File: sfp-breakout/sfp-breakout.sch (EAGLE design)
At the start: 40 parts, among them J1 694108106102, T1 BC847, T2 BC847, U1 LDO-MCP1825S, X1 PINHD-1X5LOCK, X2 PINHD-1X5LOCK, X3 PINHD-1X4LOCK

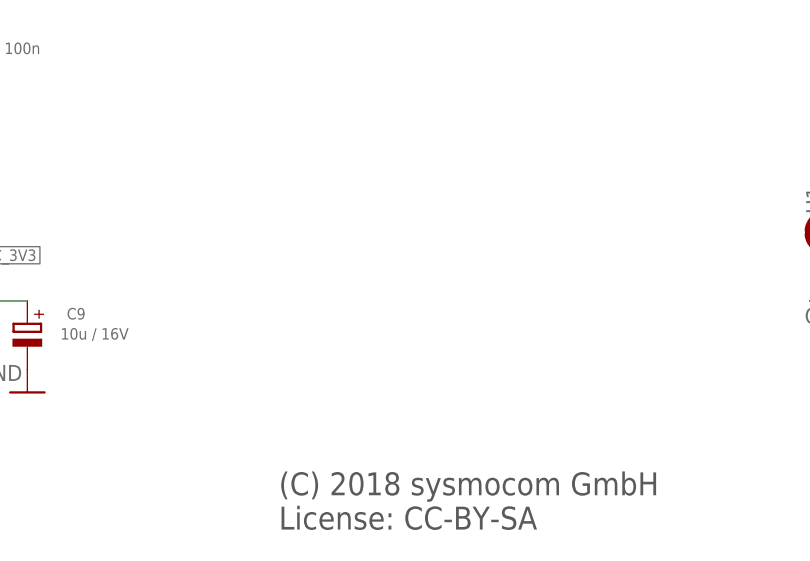
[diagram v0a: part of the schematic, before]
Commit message: sfp: add part numbers for SFP conn and cage
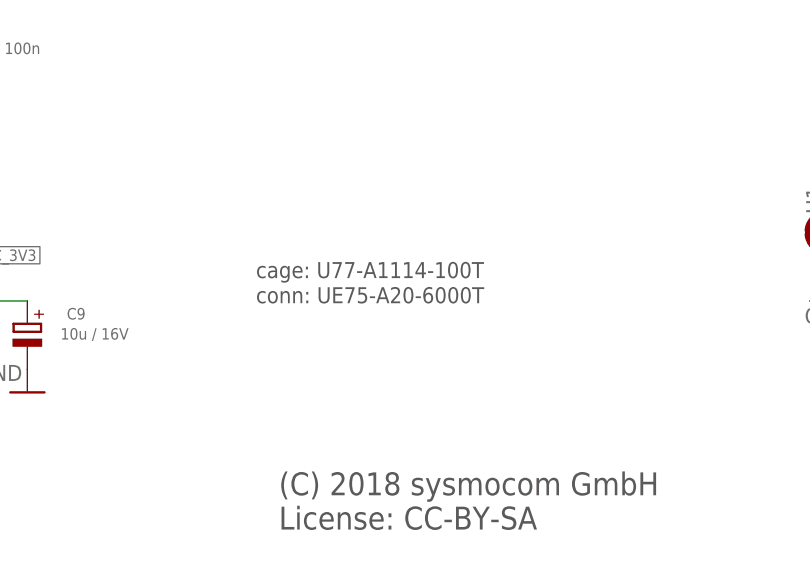
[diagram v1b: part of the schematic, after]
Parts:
- L1, L2: LINK UNKNOWN LINK -> https://www.digikey.de/product-detail/en/samsung-electro-me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
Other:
- note added: "cage: U77-A1114-100T"
- note added: "conn: UE75-A20-6000T"
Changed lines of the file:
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@@
 <attribute name="CLASS" value="INDUCTOR"/>
 <attribute name="DESCRIPTION" value="NO DESCRIPTION"/>
-<attribute name="LINK" value="UNKNOWN LINK"/>
+<attribute name="LINK" value="https://www.digikey.de/product-detail/en/samsung-electro-mechanics/CIH10T1N0SNC/1276-6301-1-ND"/>
 <attribute name="MANUFACTURER" value="UNKNOWN MANUFACTURER"/>
 <attribute name="MANUFACTURERPARTNUMBER" value="UNKNOWN MANUFACTURER PART NUMBER"/>
@@
 <attribute name="CLASS" value="INDUCTOR"/>
 <attribute name="DESCRIPTION" value="NO DESCRIPTION"/>
-<attribute name="LINK" value="UNKNOWN LINK"/>
+<attribute name="LINK" value="https://www.digikey.de/product-detail/en/samsung-electro-mechanics/CIH10T1N0SNC/1276-6301-1-ND"/>
 <attribute name="MANUFACTURER" value="UNKNOWN MANUFACTURER"/>
 <attribute name="MANUFACTURERPARTNUMBER" value="UNKNOWN MANUFACTURER PART NUMBER"/>
@@
 <text x="162.56" y="10.16" size="2.54" layer="97">(C) 2018 sysmocom GmbH
 License: CC-BY-SA</text>
+<text x="160.02" y="38.1" size="1.778" layer="97">cage: U77-A1114-100T</text>
+<text x="160.02" y="35.306" size="1.778" layer="97">conn: UE75-A20-6000T</text>
 </plain>
 <instances>

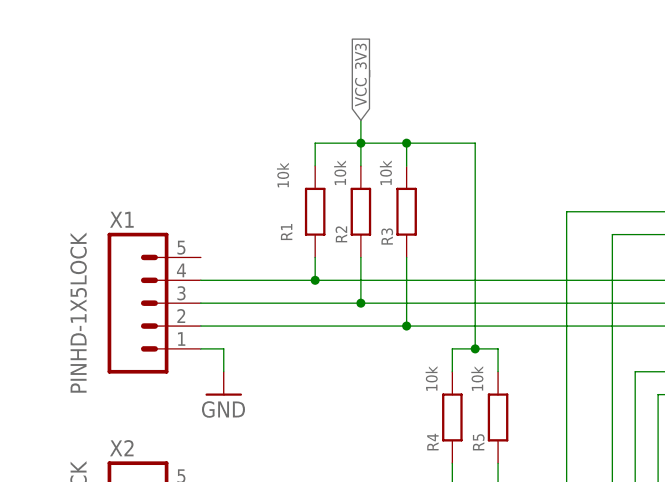
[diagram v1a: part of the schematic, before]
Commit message: sfp-breakout: X1 pin 5 missing connection to VCC_3V3
Due to an overisght, pin 5 of the X1 header was missing the intended
connection to the 3V3 plane.  Let's fix this.  No routing changes on the
PCB required, as this simply connects the VCC plane layer to the
through-hole.
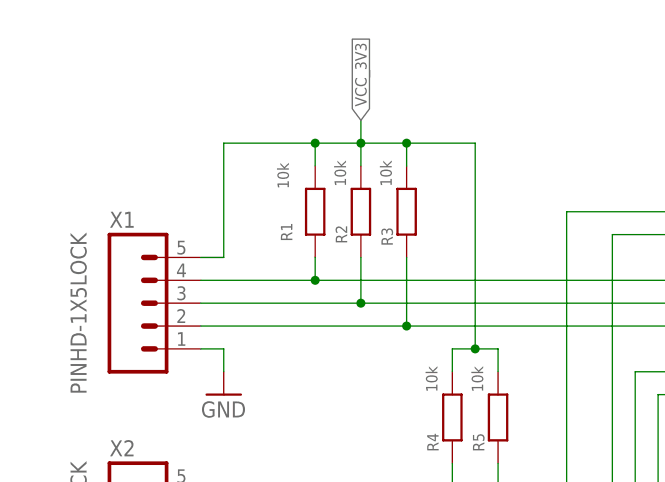
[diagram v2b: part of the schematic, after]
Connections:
- net VCC_3V3: now also X1.5
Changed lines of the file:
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@@
 <wire x1="86.36" y1="160.02" x2="78.74" y2="160.02" width="0.1524" layer="91"/>
 <junction x="78.74" y="160.02"/>
+<pinref part="X1" gate="G$1" pin="5"/>
+<wire x1="55.88" y1="147.32" x2="58.42" y2="147.32" width="0.1524" layer="91"/>
+<wire x1="58.42" y1="147.32" x2="58.42" y2="160.02" width="0.1524" layer="91"/>
+<wire x1="58.42" y1="160.02" x2="68.58" y2="160.02" width="0.1524" layer="91"/>
+<junction x="68.58" y="160.02"/>
 </segment>
 <segment>

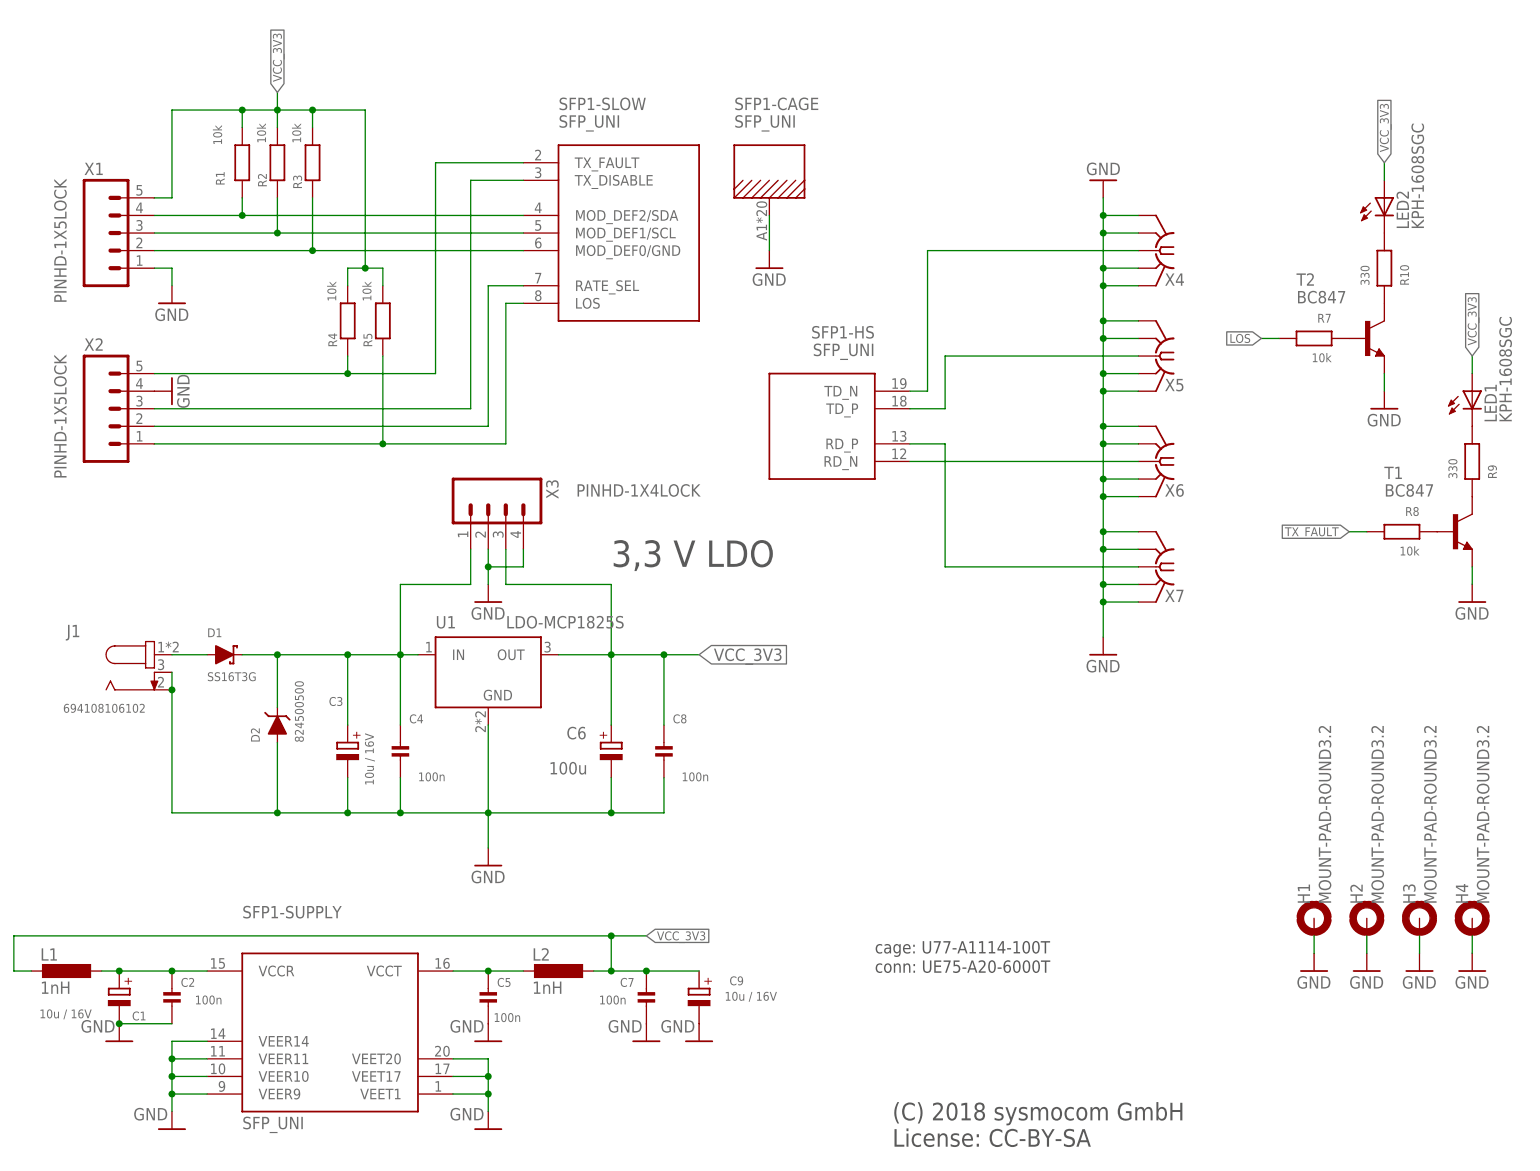
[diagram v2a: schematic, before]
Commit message: sfp-*: add OSHW logo, fill ext'd attribs for BOM
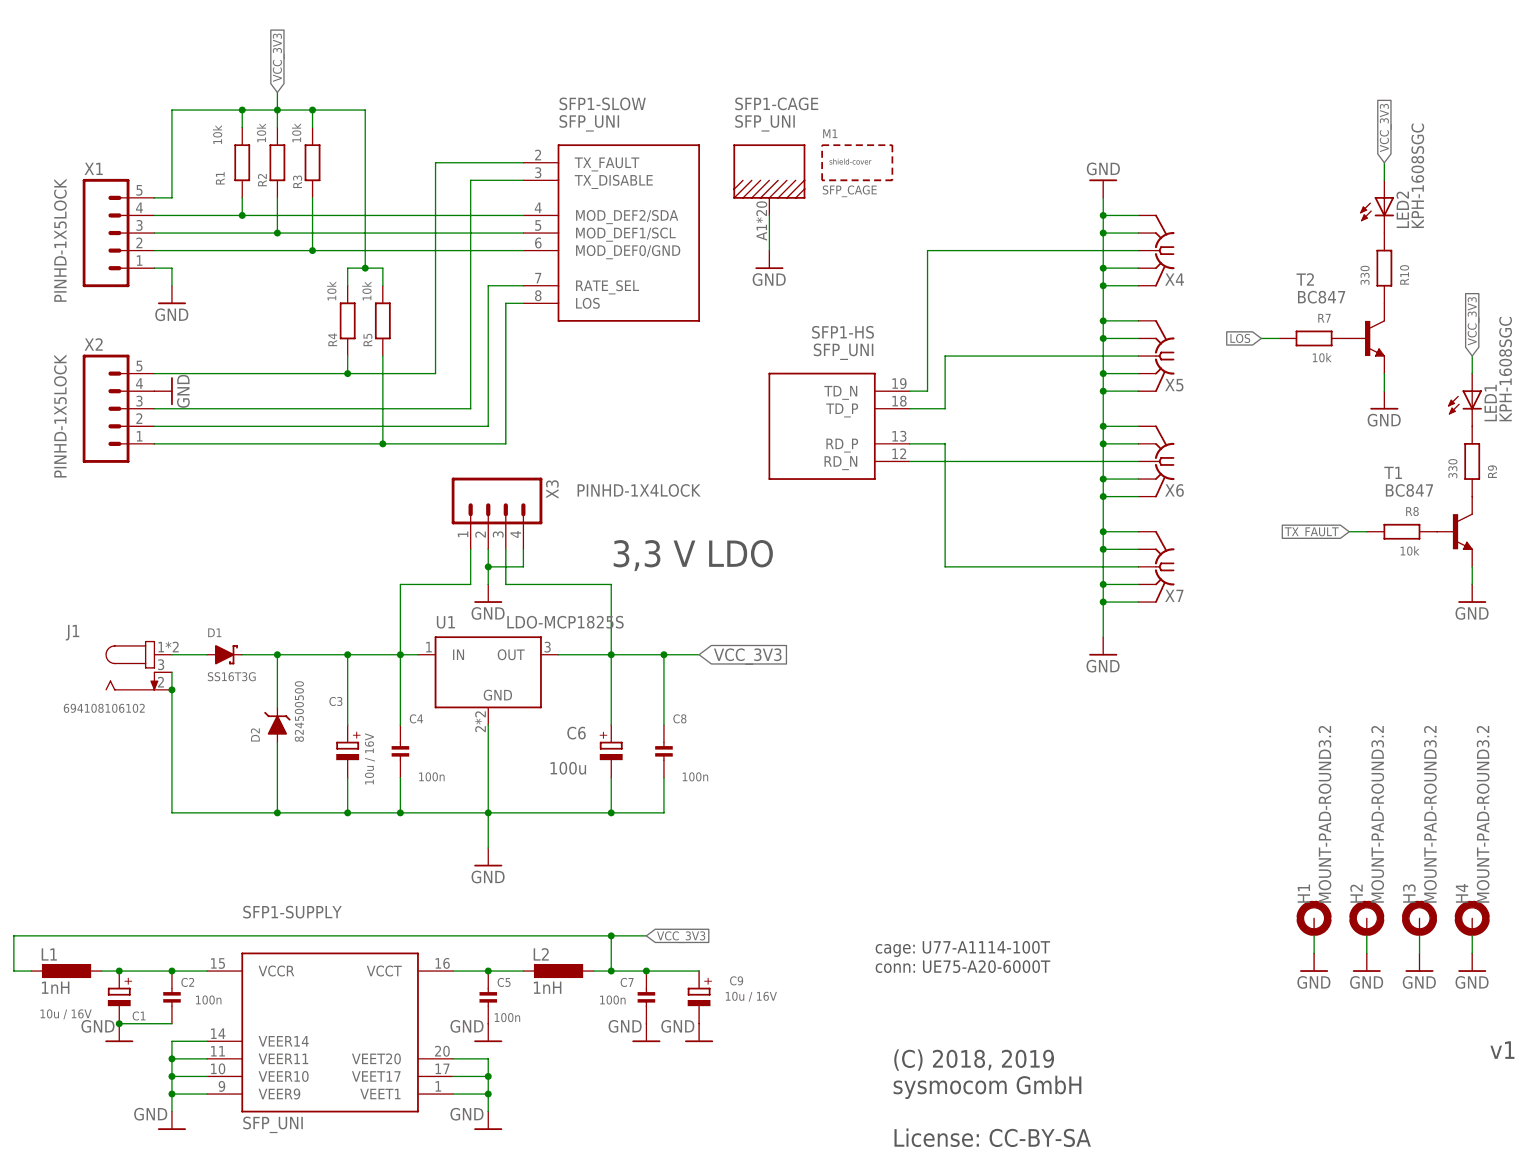
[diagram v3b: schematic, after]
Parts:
- C1, C2, C3, C4, C5, C7, C8, C9, J1, R1, R2, R3, R4, R5: ROHSCERTIFICATE UNKNOWN ROHS CERTIFICATE -> Bleifrei / RoHS-konform
- C6: DESCRIPTION CAP TANT 100UF 6.3V 10% 2413 -> CAP TANT 100UF 10%% 6.3V 2312; LINK http://www.digikey.de/product-detail/de/T491C107K006AT/399-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 -> https://www.digikey.de/product-detail/de/avx-corporation/TP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; MANUFACTURER Kemet -> AVX Corporation; MANUFACTURERPARTNUMBER T491C107K006AT -> TPSC107K006R0150; SOURCEPARTNUMBER 399-8337-1-ND -> 478-1764-1-ND
- D2: DESCRIPTION NO DESCRIPTION -> TVS DIODE 5V 9.2V DO214AC; MANUFACTURER UNKNOWN MANUFACTURER -> Wurth Electronics Inc.; MANUFACTURERPARTNUMBER UNKNOWN MANUFACTURER PART NUMBER -> 824500500; ROHSCERTIFICATE UNKNOWN ROHS CERTIFICATE -> Bleifrei / RoHS-konform; SOURCE UNKNOWN SOURCE -> DIGIKEY; SOURCEPARTNUMBER UNKNOWN SOURCE PART NUMBER -> 732-9974-1-ND
- L1, L2: DESCRIPTION NO DESCRIPTION -> FIXED IND 1NH 800MA 50 MOHM SMD; LINK https://www.digikey.de/product-detail/en/samsung-electro-me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 -> https://www.digikey.de/product-detail/de/samsung-electro-me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; MANUFACTURER UNKNOWN MANUFACTURER -> Samsung Electro-Mechanics; MANUFACTURERPARTNUMBER UNKNOWN MANUFACTURER PART NUMBER -> CIH10T1N0SNC; ROHSCERTIFICATE UNKNOWN ROHS CERTIFICATE -> Bleifrei / RoHS-konform; SOURCE UNKNOWN SOURCE -> DIGIKEY; SOURCEPARTNUMBER UNKNOWN SOURCE PART NUMBER -> 1276-6301-1-ND
- SFP1: CLASS UNKNOWN CLASS -> CONNECTOR; DESCRIPTION NO DESCRIPTION -> CONN SFP RCPT 20POS SLD R/A SMD; LINK UNKNOWN LINK -> https://www.digikey.de/product-detail/de/amphenol-icc-comme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; MANUFACTURER UNKNOWN MANUFACTURER -> Amphenol ICC (Commercial Products); MANUFACTURERPARTNUMBER UNKNOWN MANUFACTURER PART NUMBER -> UE75-A20-6000T; ROHSCERTIFICATE UNKNOWN ROHS CERTIFICATE -> Bleifrei / RoHS-konform; SOURCE UNKNOWN SOURCE -> DIGIKEY; SOURCEPARTNUMBER UNKNOWN SOURCE PART NUMBER -> UE75-A20-6000TCT-ND
- U1: DESCRIPTION NO DESCRIPTION -> IC REG LIN 3.3V 500MA SOT223-3; MANUFACTURER UNKNOWN MANUFACTURER -> Microchip Technology; MANUFACTURERPARTNUMBER UNKNOWN MANUFACTURER PART NUMBER -> MCP1825ST-3302E/DB; ROHSCERTIFICATE UNKNOWN ROHS CERTIFICATE -> Bleifrei / RoHS-konform; SOURCE UNKNOWN SOURCE -> DIGIKEY; SOURCEPARTNUMBER UNKNOWN SOURCE PART NUMBER -> MCP1825ST-3302E/DBCT-ND
- X1, X2: CLASS (none) -> CONNECTOR; DESCRIPTION (none) -> NO DESCRIPTION; LINK (none) -> UNKNOWN LINK; MANUFACTURER (none) -> UNKNOWN MANUFACTURER; MANUFACTURERPARTNUMBER (none) -> UNKNOWN MANUFACTURER PART NUMBER; POPULATED (none) -> TRUE; ROHSCERTIFICATE (none) -> UNKNOWN ROHS CERTIFICATE; SOURCE (none) -> UNKNOWN SOURCE; SOURCEPARTNUMBER (none) -> UNKNOWN SOURCE PART NUMBER
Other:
- note added: "(C) 2018, 2019 sysmocom GmbH License: CC-BY-SA"
- note removed: "(C) 2018 sysmocom GmbH License: CC-BY-SA"

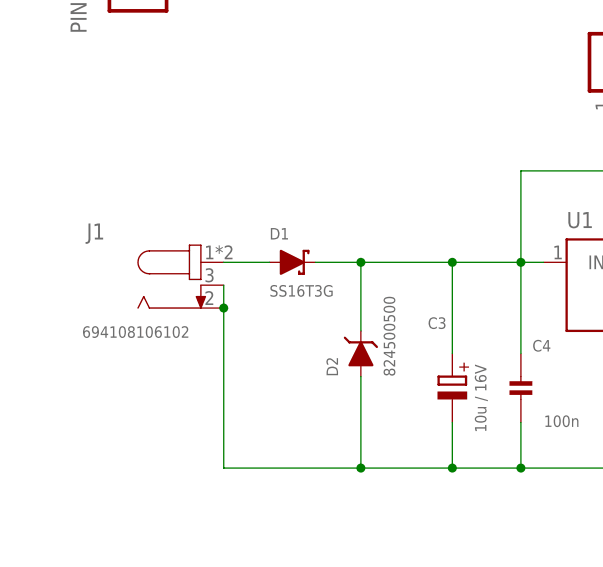
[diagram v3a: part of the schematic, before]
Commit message: sfp-breakout: update BOM attribs for availability
... for next production run
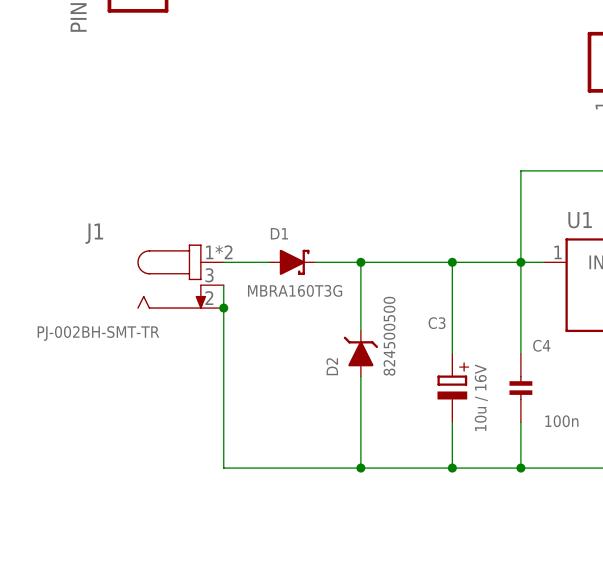
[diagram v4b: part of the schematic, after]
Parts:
- D1: value SS16T3G -> MBRA160T3G; LINK http://www.digikey.de/product-detail/de/SS16T3G/SS16T3GOSCT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 -> https://www.digikey.de/product-detail/de/on-semiconductor/M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; MANUFACTURERPARTNUMBER SS16T3G -> MBRA160T3G; ROHSCERTIFICATE Bleifrei / RoHS-konform -> RoHS3-konform; SOURCEPARTNUMBER SS16T3GOSCT-ND -> MBRA160T3GOSCT-ND
- J1: value 694108106102 -> PJ-002BH-SMT-TR; CLASS CONNECTOR\JUMPER -> CONNECTOR; LINK https://www.digikey.de/product-detail/de/wurth-electronics-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 -> https://www.digikey.de/product-detail/de/cui-inc/PJ-002BH-S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; MANUFACTURER Wurth Electronics Inc. -> CUI Devices; MANUFACTURERPARTNUMBER 694108106102 -> PJ-002BH-SMT-TR; ROHSCERTIFICATE Bleifrei / RoHS-konform -> RoHS-konform; SOURCEPARTNUMBER 732-5933-1-ND -> CP-002BHPJCT-ND
- L1, L2: DESCRIPTION FIXED IND 1NH 800MA 50 MOHM SMD -> FIXED IND 1NH 500MA 50 MOHM SMD; LINK https://www.digikey.de/product-detail/de/samsung-electro-me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 -> https://www.digikey.de/product-detail/de/abracon-llc/AIMC-0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; MANUFACTURER Samsung Electro-Mechanics -> Abracon LLC; MANUFACTURERPARTNUMBER CIH10T1N0SNC -> AIMC-0603-1N0S-T; ROHSCERTIFICATE Bleifrei / RoHS-konform -> RoHS-konform; SOURCEPARTNUMBER 1276-6301-1-ND -> 535-11529-1-ND
- R1, R2, R3, R4, R5: MANUFACTURER Stackpole Electronics Inc. -> Stackpole Electronics Inc; ROHSCERTIFICATE Bleifrei / RoHS-konform -> RoHS3-konform
- R10, R9: DESCRIPTION RES 330 OHM 1/10W 1% 0603 SMD -> RES SMD 330 OHM 1%% 1/10W 0603; LINK http://www.digikey.de/product-detail/de/foo/RHM330CFCT-ND -> https://www.digikey.de/product-detail/de/yageo/RC0603FR-073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; MANUFACTURER Rohm Semiconductor -> Yageo; MANUFACTURERPARTNUMBER MCR03ERTF3300 -> RC0603FR-07330RL; ROHSCERTIFICATE Bleifrei / RoHS-konform -> RoHS3-konform; SOURCEPARTNUMBER RHM330CFCT-ND -> 311-330HRCT-ND
- R7, R8: DESCRIPTION RES 10K OHM 1/10W 1% 0603 SMD -> RES 10K OHM 1%% 1/10W 0603; LINK http://www.digikey.de/product-detail/de/foo/RHM10.0KCFCT-ND -> https://www.digikey.de/product-detail/de/stackpole-electron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; MANUFACTURER Rohm Semiconductor -> Stackpole Electronics Inc; MANUFACTURERPARTNUMBER MCR03ERTF1002 -> RMCF0603FT10K0; ROHSCERTIFICATE Bleifrei / RoHS-konform -> RoHS3-konform; SOURCEPARTNUMBER RHM10.0KCFCT-ND -> RMCF0603FT10K0CT-ND
- T1, T2: DESCRIPTION TRANS NPN GP 100MA 45V SOT23 -> TRANS NPN 45V 0.1A SOT23; LINK http://www.digikey.de/product-detail/de/foo/568-1636-1-ND -> https://www.digikey.de/product-detail/de/nexperia-usa-inc/B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; MANUFACTURER NXP Semiconductors -> Nexperia USA Inc.; ROHSCERTIFICATE Bleifrei / RoHS-konform -> RoHS3-konform; SOURCEPARTNUMBER 568-1636-1-ND -> 1727-2924-1-ND
